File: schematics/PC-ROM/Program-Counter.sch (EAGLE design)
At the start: 33 parts

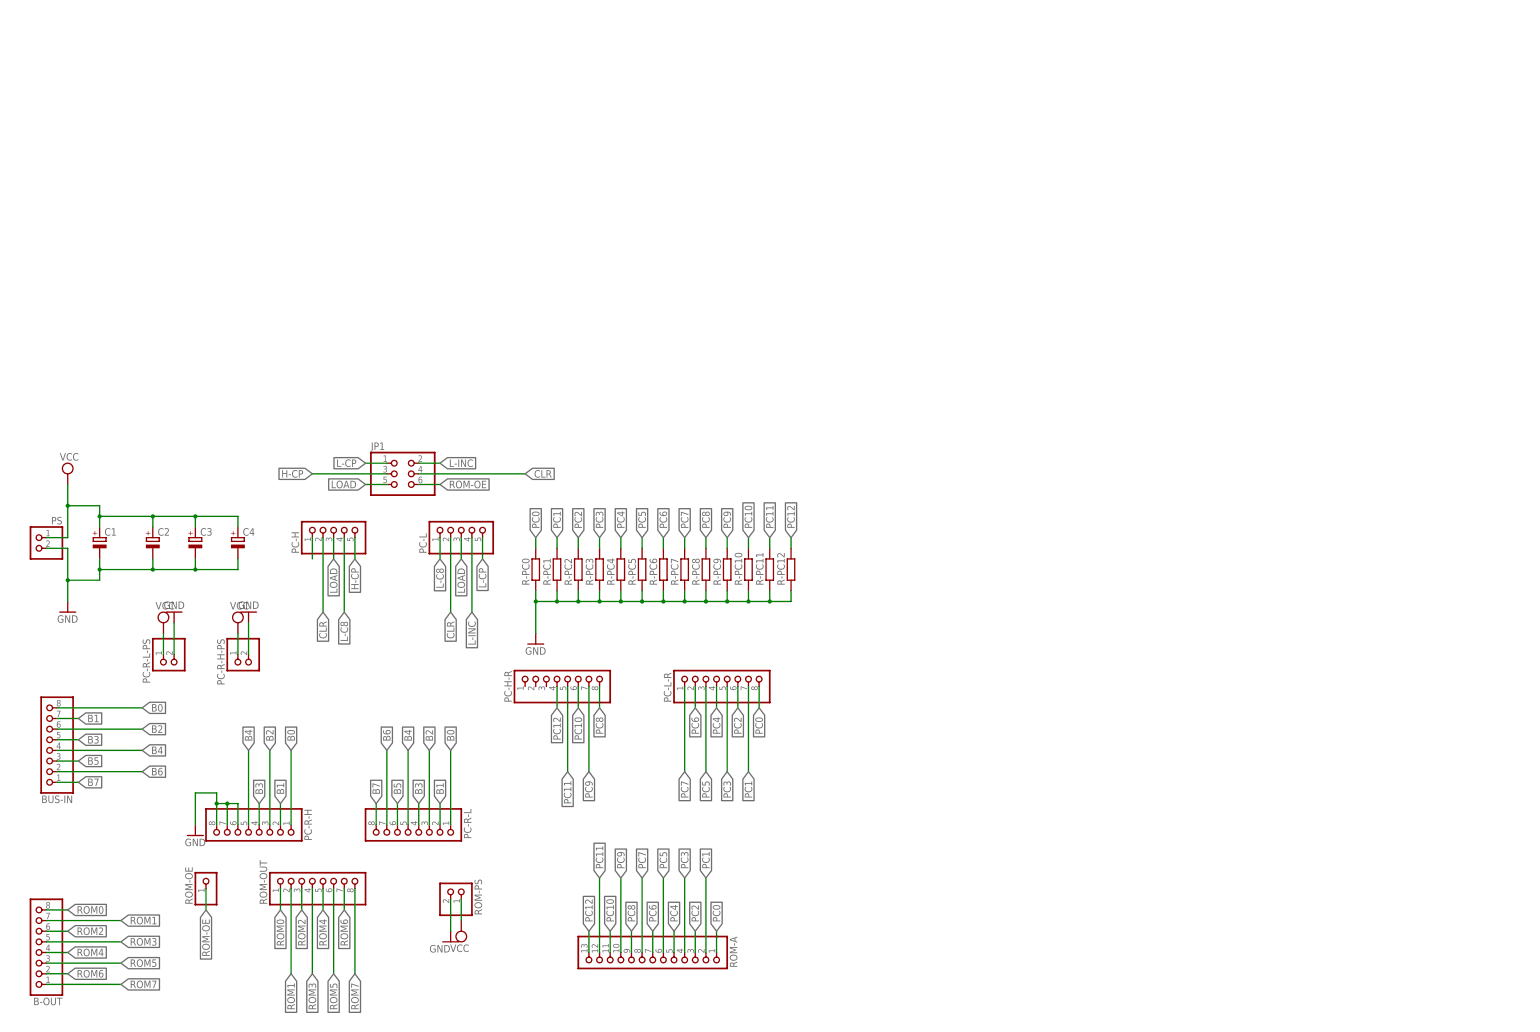
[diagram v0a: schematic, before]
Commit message: PC can now output to bus. Merged PC, PC-Bus and ROM.
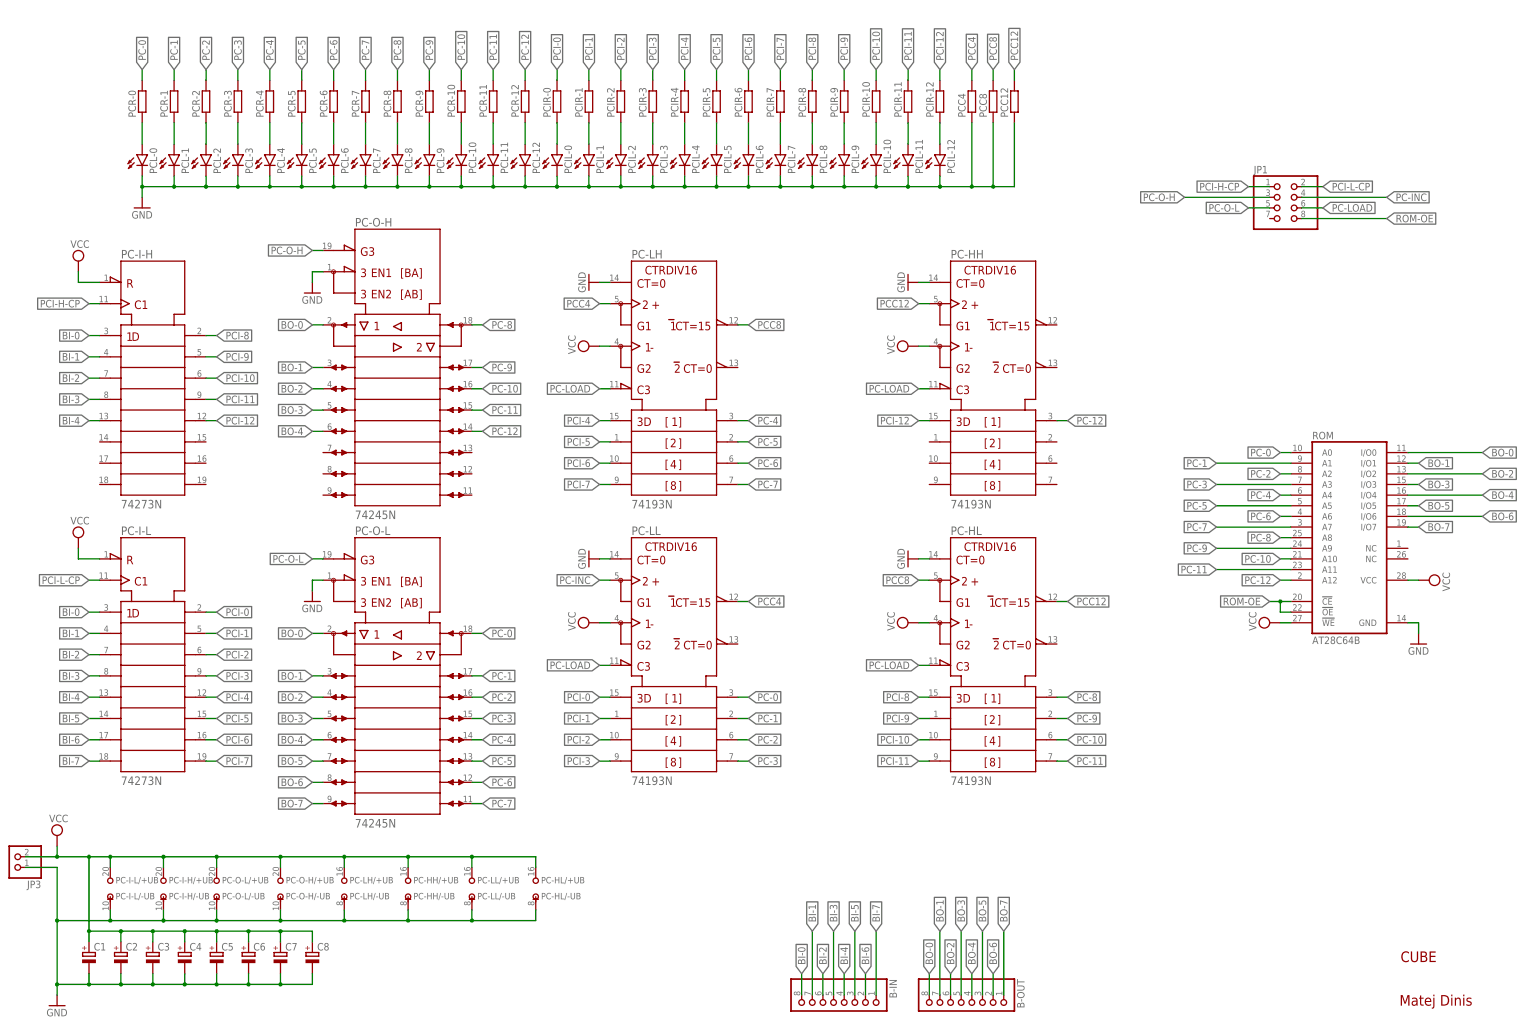
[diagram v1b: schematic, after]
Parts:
- removed BUS-IN, PC-H-R, PC-L-R, PC-R-H, PC-R-L, ROM-OUT: (no value), pinhead:PINHD-1X8
- removed PC-H, PC-L: (no value), pinhead:PINHD-1X5
- removed PC-R-H-PS, PC-R-L-PS, PS, ROM-PS: (no value), pinhead:PINHD-1X2
- removed R-PC0, R-PC1, R-PC10, R-PC11, R-PC12, R-PC2, R-PC3, R-PC4, R-PC5, R-PC6, R-PC7, R-PC8, R-PC9: (no value), rcl:R-EU_0204/7
- removed ROM-A: (no value), pinhead:PINHD-1X13
- removed ROM-OE: (no value), pinhead:PINHD-1X1
- added B-IN: (no value), pinhead:PINHD-1X8
- added C5, C6, C7, C8: (no value), rcl:CPOL-EUE3.5-8
- added JP3: (no value), pinhead:PINHD-1X2
- added PC-HH, PC-HL, PC-LH, PC-LL: 74193N, 74ttl-din:74193N
- added PC-I-H, PC-I-L: 74273N, 74ttl-din:74273N
- added PC-O-H, PC-O-L: 74245N, 74ttl-din:74245N
- added PCC12, PCC4, PCC8, PCIR-0, PCIR-1, PCIR-10, PCIR-11, PCIR-12, PCIR-2, PCIR-3, PCIR-4, PCIR-5, PCIR-6, PCIR-7, PCIR-8, PCIR-9, PCR-0, PCR-1, PCR-10, PCR-11, PCR-12, PCR-2, PCR-3, PCR-4, PCR-5, PCR-6, PCR-7, PCR-8, PCR-9: (no value), rcl:R-EU_0207/10
- added PCIL-0, PCIL-1, PCIL-10, PCIL-11, PCIL-12, PCIL-2, PCIL-3, PCIL-4, PCIL-5, PCIL-6, PCIL-7, PCIL-8, PCIL-9, PCL-0, PCL-1, PCL-10, PCL-11, PCL-12, PCL-2, PCL-3, PCL-4, PCL-5, PCL-6, PCL-7, PCL-8, PCL-9: (no value), led:LED5MM
- added ROM: AT28C64B, memory-nec:28C64C
- JP1: device pinhead:PINHD-2X3 -> pinhead:PINHD-2X4
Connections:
- removed net B0: BUS-IN.8, PC-R-H.1, PC-R-L.1
- removed net B1: BUS-IN.7, PC-R-H.2, PC-R-L.2
- removed net B2: BUS-IN.6, PC-R-H.3, PC-R-L.3
- removed net B3: BUS-IN.5, PC-R-H.4, PC-R-L.4
- removed net B4: BUS-IN.4, PC-R-H.5, PC-R-L.5
- removed net B5: BUS-IN.3, PC-R-L.6
- removed net B6: BUS-IN.2, PC-R-L.7
- removed net B7: BUS-IN.1, PC-R-L.8
- removed net CLR: JP1.4, PC-H.2, PC-L.2
- removed net H-C8: PC-H.1
- removed net H-CP: JP1.3, PC-H.5
- removed net L-C8: PC-H.4, PC-L.1
- removed net L-CP: JP1.1, PC-L.5
- removed net L-INC: JP1.2, PC-L.4
- removed net LOAD: JP1.5, PC-H.3, PC-L.3
- removed net PC0: PC-L-R.8, R-PC0.2, ROM-A.1
- removed net PC1: PC-L-R.7, R-PC1.2, ROM-A.2
- removed net PC10: PC-H-R.6, R-PC10.2, ROM-A.11
- removed net PC11: PC-H-R.5, R-PC11.2, ROM-A.12
- removed net PC12: PC-H-R.4, R-PC12.2, ROM-A.13
- removed net PC2: PC-L-R.6, R-PC2.2, ROM-A.3
- removed net PC3: PC-L-R.5, R-PC3.2, ROM-A.4
- removed net PC4: PC-L-R.4, R-PC4.2, ROM-A.5
- removed net PC5: PC-L-R.3, R-PC5.2, ROM-A.6
- removed net PC6: PC-L-R.2, R-PC6.2, ROM-A.7
- removed net PC7: PC-L-R.1, R-PC7.2, ROM-A.8
- removed net PC8: PC-H-R.8, R-PC8.2, ROM-A.9
- removed net PC9: PC-H-R.7, R-PC9.2, ROM-A.10
- removed net ROM0: B-OUT.8, ROM-OUT.1
- removed net ROM1: B-OUT.7, ROM-OUT.2
- removed net ROM2: B-OUT.6, ROM-OUT.3
- removed net ROM3: B-OUT.5, ROM-OUT.4
- removed net ROM4: B-OUT.4, ROM-OUT.5
- removed net ROM5: B-OUT.3, ROM-OUT.6
- removed net ROM6: B-OUT.2, ROM-OUT.7
- removed net ROM7: B-OUT.1, ROM-OUT.8
- new net BI-0: B-IN.8, PC-I-H1.1D, PC-I-L1.1D
- new net BI-1: B-IN.7, PC-I-H1.2D, PC-I-L1.2D
- new net BI-2: B-IN.6, PC-I-H1.3D, PC-I-L1.3D
- new net BI-3: B-IN.5, PC-I-H1.4D, PC-I-L1.4D
- new net BI-4: B-IN.4, PC-I-H1.5D, PC-I-L1.5D
- new net BI-5: B-IN.3, PC-I-L1.6D
- new net BI-6: B-IN.2, PC-I-L1.7D
- new net BI-7: B-IN.1, PC-I-L1.8D
- new net BO-0: B-OUT.8, PC-O-H1.A1, PC-O-L1.A1, ROM.I/O0
- new net BO-1: B-OUT.7, PC-O-H1.A2, PC-O-L1.A2, ROM.I/O1
- new net BO-2: B-OUT.6, PC-O-H1.A3, PC-O-L1.A3, ROM.I/O2
- new net BO-3: B-OUT.5, PC-O-H1.A4, PC-O-L1.A4, ROM.I/O3
- new net BO-4: B-OUT.4, PC-O-H1.A5, PC-O-L1.A5, ROM.I/O4
- new net BO-5: B-OUT.3, PC-O-L1.A6, ROM.I/O5
- new net BO-6: B-OUT.2, PC-O-L1.A7, ROM.I/O6
- new net BO-7: B-OUT.1, PC-O-L1.A8, ROM.I/O7
- new net N$1: PCL-0.A, PCR-0.1
- new net N$10: PCL-3.A, PCR-3.1
- new net N$13: PCL-4.A, PCR-4.1
- new net N$16: PCL-5.A, PCR-5.1
- new net N$21: PCL-6.A, PCR-6.1
- new net N$24: PCL-7.A, PCR-7.1
- new net N$27: PCL-8.A, PCR-8.1
- new net N$30: PCL-9.A, PCR-9.1
- new net N$33: PCL-10.A, PCR-10.1
- new net N$38: PCL-11.A, PCR-11.1
- new net N$4: PCL-1.A, PCR-1.1
- new net N$41: PCL-12.A, PCR-12.1
- new net N$44: PCIL-0.A, PCIR-0.1
- new net N$47: PCIL-1.A, PCIR-1.1
- new net N$50: PCIL-2.A, PCIR-2.1
- new net N$55: PCIL-3.A, PCIR-3.1
- new net N$58: PCIL-4.A, PCIR-4.1
- new net N$61: PCIL-5.A, PCIR-5.1
- new net N$64: PCIL-6.A, PCIR-6.1
- new net N$67: PCIL-7.A, PCIR-7.1
- new net N$7: PCL-2.A, PCR-2.1
- new net N$70: PCIL-8.A, PCIR-8.1
- new net N$73: PCIL-9.A, PCIR-9.1
- new net N$76: PCIL-10.A, PCIR-10.1
- new net N$79: PCIL-11.A, PCIR-11.1
- new net N$82: PCIL-12.A, PCIR-12.1
- new net PC-0: PC-LL1.QA, PC-O-L1.B1, PCR-0.2, ROM.A0
- new net PC-1: PC-LL1.QB, PC-O-L1.B2, PCR-1.2, ROM.A1
- new net PC-10: PC-HL1.QC, PC-O-H1.B3, PCR-10.2, ROM.A10
- new net PC-11: PC-HL1.QD, PC-O-H1.B4, PCR-11.2, ROM.A11
- new net PC-12: PC-HH1.QA, PC-O-H1.B5, PCR-12.2, ROM.A12
- new net PC-2: PC-LL1.QC, PC-O-L1.B3, PCR-2.2, ROM.A2
- new net PC-3: PC-LL1.QD, PC-O-L1.B4, PCR-3.2, ROM.A3
- new net PC-4: PC-LH1.QA, PC-O-L1.B5, PCR-4.2, ROM.A4
- new net PC-5: PC-LH1.QB, PC-O-L1.B6, PCR-5.2, ROM.A5
- new net PC-6: PC-LH1.QC, PC-O-L1.B7, PCR-6.2, ROM.A6
- new net PC-7: PC-LH1.QD, PC-O-L1.B8, PCR-7.2, ROM.A7
- new net PC-8: PC-HL1.QA, PC-O-H1.B1, PCR-8.2, ROM.A8
- new net PC-9: PC-HL1.QB, PC-O-H1.B2, PCR-9.2, ROM.A9
- new net PC-INC: JP1.4, PC-LL1.UP
- new net PC-LOAD: JP1.6, PC-HH1.!LOAD, PC-HL1.!LOAD, PC-LH1.!LOAD, PC-LL1.!LOAD
- new net PC-O-H: JP1.3, PC-O-H1.!G
- new net PC-O-L: JP1.5, PC-O-L1.!G
- new net PCC12: PC-HH1.UP, PC-HL1.!CO, PCC12.2
- new net PCC4: PC-LH1.UP, PC-LL1.!CO, PCC4.2
- new net PCC8: PC-HL1.UP, PC-LH1.!CO, PCC8.2
- new net PCI-0: PC-I-L1.1Q, PC-LL1.A, PCIR-0.2
- new net PCI-1: PC-I-L1.2Q, PC-LL1.B, PCIR-1.2
- new net PCI-10: PC-HL1.C, PC-I-H1.3Q, PCIR-10.2
- new net PCI-11: PC-HL1.D, PC-I-H1.4Q, PCIR-11.2
- new net PCI-12: PC-HH1.A, PC-I-H1.5Q, PCIR-12.2
- new net PCI-2: PC-I-L1.3Q, PC-LL1.C, PCIR-2.2
- new net PCI-3: PC-I-L1.4Q, PC-LL1.D, PCIR-3.2
- new net PCI-4: PC-I-L1.5Q, PC-LH1.A, PCIR-4.2
- new net PCI-5: PC-I-L1.6Q, PC-LH1.B, PCIR-5.2
- new net PCI-6: PC-I-L1.7Q, PC-LH1.C, PCIR-6.2
- new net PCI-7: PC-I-L1.8Q, PC-LH1.D, PCIR-7.2
- new net PCI-8: PC-HL1.A, PC-I-H1.1Q, PCIR-8.2
- new net PCI-9: PC-HL1.B, PC-I-H1.2Q, PCIR-9.2
- new net PCI-H-CP: JP1.1, PC-I-H1.CLK
- new net PCI-L-CP: JP1.2, PC-I-L1.CLK
- net GND: now also C5.-, C6.-, C7.-, C8.-, JP3.1, PC-HH/-UB.-UB, PC-HH1.CLR, PC-HL/-UB.-UB, PC-HL1.CLR, PC-I-H/-UB.-UB, PC-I-L/-UB.-UB, PC-LH/-UB.-UB, PC-LH1.CLR, PC-LL/-UB.-UB, PC-LL1.CLR, PC-O-H/-UB.-UB, PC-O-H1.DIR, PC-O-L/-UB.-UB, PC-O-L1.DIR, PCC12.1, PCC4.1, PCC8.1, PCIL-0.C, PCIL-1.C, PCIL-10.C, PCIL-11.C, PCIL-12.C, PCIL-2.C, PCIL-3.C, PCIL-4.C, PCIL-5.C, PCIL-6.C, PCIL-7.C, PCIL-8.C, PCIL-9.C, PCL-0.C, PCL-1.C, PCL-10.C, PCL-11.C, PCL-12.C, PCL-2.C, PCL-3.C, PCL-4.C, PCL-5.C, PCL-6.C, PCL-7.C, PCL-8.C, PCL-9.C, ROM.GND; no longer PC-R-H-PS.2, PC-R-H.6, PC-R-H.7, PC-R-H.8, PC-R-L-PS.2, PS.2, R-PC0.1, R-PC1.1, R-PC10.1, R-PC11.1, R-PC12.1, R-PC2.1, R-PC3.1, R-PC4.1, R-PC5.1, R-PC6.1, R-PC7.1, R-PC8.1, R-PC9.1, ROM-PS.2
- net ROM-OE: now also JP1.8, ROM.!CE, ROM.!OE; no longer JP1.6, ROM-OE.1
- net VCC: now also C5.+, C6.+, C7.+, C8.+, JP3.2, PC-HH/+UB.+UB, PC-HH1.DOWN, PC-HL/+UB.+UB, PC-HL1.DOWN, PC-I-H/+UB.+UB, PC-I-H1.!CLR, PC-I-L/+UB.+UB, PC-I-L1.!CLR, PC-LH/+UB.+UB, PC-LH1.DOWN, PC-LL/+UB.+UB, PC-LL1.DOWN, PC-O-H/+UB.+UB, PC-O-L/+UB.+UB, ROM.!WE, ROM.VCC; no longer PC-R-H-PS.1, PC-R-L-PS.1, PS.1, ROM-PS.1
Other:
- note added: "CUBE"
- note added: "Matej Dinis"
- moved on the sheet: B-OUT, C1, C2, C3, C4
